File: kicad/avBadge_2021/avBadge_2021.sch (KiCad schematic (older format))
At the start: 36 parts, among them J1 AVR-ISP-6, Q1 2N3904, SW1 SW_Push_Dual, SW2 SW_SPDT, U1 ATtiny84A-SSU

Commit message: arduino code updates and manufactured v01 gerbers completed.
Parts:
- Q1: footprint TO_SOT_Packages_SMD:SOT-23 -> aerospace_badge:SOT-23-NPN
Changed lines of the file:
@@
 F 0 "Q1" H 8490 5046 50  0000 L CNN
 F 1 "2N3904" H 8490 4955 50  0000 L CNN
-F 2 "TO_SOT_Packages_SMD:SOT-23" H 8500 4925 50  0001 L CIN
+F 2 "aerospace_badge:SOT-23-NPN" H 8500 4925 50  0001 L CIN
 F 3 "https://www.fairchildsemi.com/datasheets/2N/2N3904.pdf" H 8300 5000 50  0001 L CNN
 	1    8300 5000

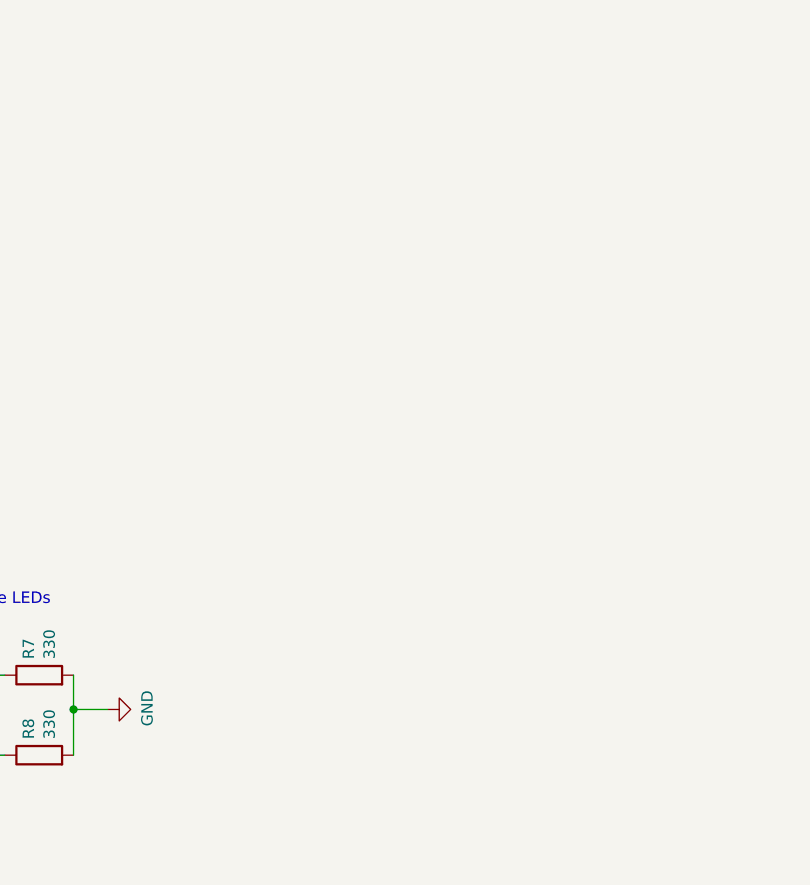
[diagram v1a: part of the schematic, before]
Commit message: arduino update to include pulsing lights as desired.
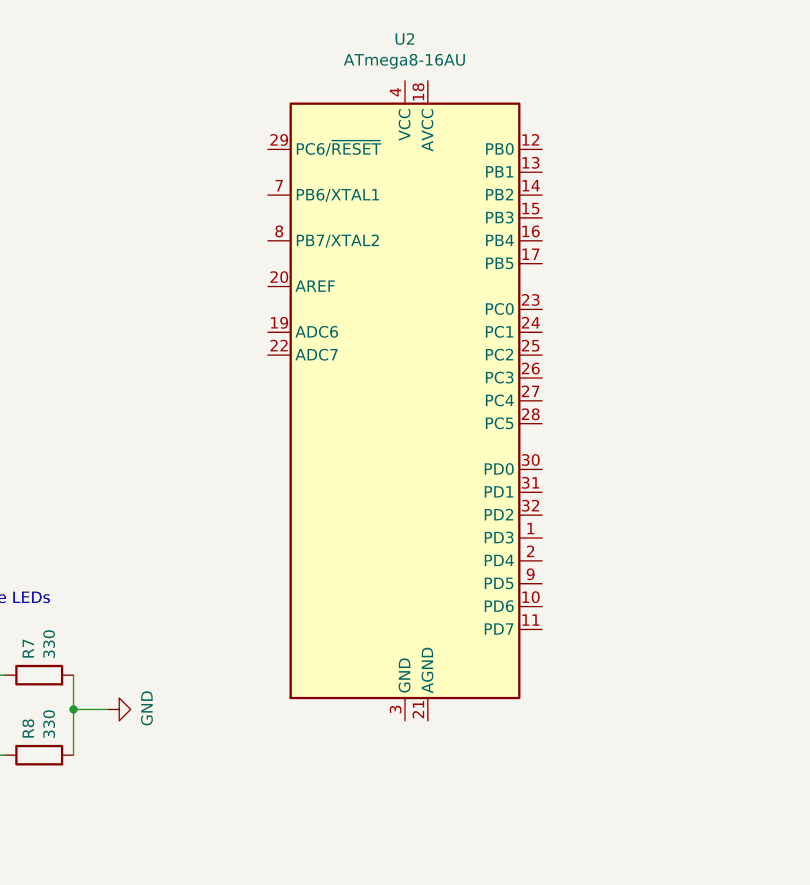
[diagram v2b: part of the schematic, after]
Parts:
- added U2: ATmega8-16AU, Package_QFP:TQFP-32_7x7mm_P0.8mm, symbol MCU_Microchip_ATmega:ATmega8-16AU
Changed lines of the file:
@@
 Wire Wire Line
 	3250 4800 3450 4800
+$Comp
+L MCU_Microchip_ATmega:ATmega8-16AU U2
+U 1 1 608E9FF1
+P 9300 2250
+F 0 "U2" H 9300 3831 50  0000 C CNN
+F 1 "ATmega8-16AU" H 9300 3740 50  0000 C CNN
+F 2 "Package_QFP:TQFP-32_7x7mm_P0.8mm" H 9300 2250 50  0001 C CIN
+F 3 "http://ww1.microchip.com/downloads/en/DeviceDoc/atmel-2486-8-bit-avr-microcontroller-atmega8_l_datasheet.pdf" H 9300 2250 50  0001 C CNN
+	1    9300 2250
+	1    0    0    -1
+$EndComp
 $EndSCHEMATC

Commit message: refactor of kicad files working through incorporation of art and new MCU design.
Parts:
- removed D1, D2: APFA3010, sunled:XZMDKCBDDG45S-9, symbol LED:APFA3010
- removed SW1: SW_Push_Dual, aerospace_badge:FSMCTTR, symbol Switch:SW_Push_Dual
- removed U1: ATtiny84A-SSU, aerospace_badge:attiny84, symbol MCU_Microchip_ATtiny:ATtiny84A-SSU
- added D1, D2: SunLED_RGB_ReverseMount, sunled:XZMDKCBDDG45S-9, symbol LED:SunLED_RGB_ReverseMount
- added D4: LED, sunled:XZDGK45WT-9, symbol Device:LED
- added P1: SerialConnector, aerospace_badge:serialConnector, symbol avBadge_symbols:SerialConnector
- added R11: 330, Resistors_SMD:R_1206_3216Metric, symbol Device:R
- added R12, R7: 10K, Resistors_SMD:R_1206_3216Metric, symbol Device:R
- added S1: OpenConnections, symbol avBadge_symbols:OpenConnections
- added VR1: TLV702, TO_SOT_Packages_SMD:SOT-23-5, symbol avBadge_symbols:TLV702
- BT1: footprint Battery:BatteryHolder_Keystone_3034_1x20mm -> aerospace_badge:BHX2-2032
- D10: renamed from D9; footprint aerospace_badge:led_in-s124ar -> sunled:XZM2CRK45WT-9
- D11: renamed from D10; footprint aerospace_badge:led_in-s124ar -> sunled:XZM2CRK45WT-9
- D12: renamed from D11; footprint aerospace_badge:led_in-s124ar -> sunled:XZM2CRK45WT-9
- U1: renamed from U2; footprint Package_QFP:TQFP-32_7x7mm_P0.8mm -> digikey-footprints:TQFP-32_7x7mm
- renumbered D4 to D5, D5 to D6, D6 to D7, D7 to D8, D8 to D9, R2 to R1, R8 to R10, R10 to R13, R11 to R14, R12 to R15, R13 to R16, R14 to R17, R15 to R18, R16 to R19, R1 to R2, R17 to R20, R4 to R3, R3 to R4, R6 to R5, R5 to R6, R7 to R8, SW2 to SW1
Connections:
- wire segments 93 -> 125
- no-connect marks 4 -> 12
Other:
- note added: "Lost Comms Interrupt"
- note added: "PCL Interrupt"
- note added: "Runway Lighting (Red, Green, Yellow)"
- note added: "UFO"
- note added: "UFO Trigger"
- note removed: "Runway Lighting (Red, Green, White)"
- moved on the sheet: BT1, C1, C2, D10, D11, D12, D6, D7, D8, D9, J1, Q1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

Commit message: v0.2 gerber builtout and sent for fabrication.
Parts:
- D10, D11, D12: footprint sunled:XZM2CRK45WT-9 -> sunled:XZMYK45WT-9
- D6, D7: footprint sunled:XZDGK45WT-9 -> sunled:XZM2CRK45WT-9
- D8, D9: footprint sunled:XZM2CRK45WT-9 -> sunled:XZDGK45WT-9
- P1: symbol avBadge_symbols:SerialConnector -> avBadge_2021-rescue:SerialConnector-avBadge_symbols
- S1: footprint (none) -> aerospace_badge:artboard
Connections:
- net GND: now also P1.~ (GND); no longer P1.3 (GND)
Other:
- note added: "G"
- note added: "R"
- note added: "Y"
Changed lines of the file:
@@
 F 0 "D6" H 7443 5567 50  0000 C CNN
 F 1 "LED" H 7443 5476 50  0000 C CNN
-F 2 "sunled:XZDGK45WT-9" H 7450 5350 50  0001 C CNN
+F 2 "sunled:XZM2CRK45WT-9" H 7450 5350 50  0001 C CNN
 F 3 "~" H 7450 5350 50  0001 C CNN
 	1    7450 5350
@@
 F 0 "D7" H 7843 5567 50  0000 C CNN
 F 1 "LED" H 7843 5476 50  0000 C CNN
-F 2 "sunled:XZDGK45WT-9" H 7850 5350 50  0001 C CNN
+F 2 "sunled:XZM2CRK45WT-9" H 7850 5350 50  0001 C CNN
 F 3 "~" H 7850 5350 50  0001 C CNN
 	1    7850 5350
@@
 F 0 "D8" H 8193 5567 50  0000 C CNN
 F 1 "LED" H 8193 5476 50  0000 C CNN
-F 2 "sunled:XZM2CRK45WT-9" H 8200 5350 50  0001 C CNN
+F 2 "sunled:XZDGK45WT-9" H 8200 5350 50  0001 C CNN
 F 3 "~" H 8200 5350 50  0001 C CNN
 	1    8200 5350
@@
 F 0 "D9" H 8543 5567 50  0000 C CNN
 F 1 "LED" H 8543 5476 50  0000 C CNN
-F 2 "sunled:XZM2CRK45WT-9" H 8550 5350 50  0001 C CNN
+F 2 "sunled:XZDGK45WT-9" H 8550 5350 50  0001 C CNN
 F 3 "~" H 8550 5350 50  0001 C CNN
 	1    8550 5350
@@
 F 0 "D10" H 8893 5567 50  0000 C CNN
 F 1 "LED" H 8893 5476 50  0000 C CNN
-F 2 "sunled:XZM2CRK45WT-9" H 8900 5350 50  0001 C CNN
+F 2 "sunled:XZMYK45WT-9" H 8900 5350 50  0001 C CNN
 F 3 "~" H 8900 5350 50  0001 C CNN
 	1    8900 5350
@@
 F 0 "D11" H 9243 5567 50  0000 C CNN
 F 1 "LED" H 9243 5476 50  0000 C CNN
-F 2 "sunled:XZM2CRK45WT-9" H 9250 5350 50  0001 C CNN
+F 2 "sunled:XZMYK45WT-9" H 9250 5350 50  0001 C CNN
 F 3 "~" H 9250 5350 50  0001 C CNN
 	1    9250 5350
@@
 F 0 "D12" H 9543 5567 50  0000 C CNN
 F 1 "LED" H 9543 5476 50  0000 C CNN
-F 2 "sunled:XZM2CRK45WT-9" H 9550 5350 50  0001 C CNN
+F 2 "sunled:XZMYK45WT-9" H 9550 5350 50  0001 C CNN
 F 3 "~" H 9550 5350 50  0001 C CNN
 	1    9550 5350
@@
 	4500 1850 4750 1850
 $Comp
-L avBadge_symbols:SerialConnector P1
+L avBadge_2021-rescue:SerialConnector-avBadge_symbols P1
 U 1 1 60B5934D
 P 3700 5500
@@
 F 0 "S1" H 5625 3925 50  0000 C CNN
 F 1 "OpenConnections" H 5625 3834 50  0000 C CNN
-F 2 "" H 5550 3700 50  0001 C CNN
+F 2 "aerospace_badge:artboard" H 5550 3700 50  0001 C CNN
 F 3 "" H 5550 3700 50  0001 C CNN
 	1    5550 3700
@@
 Wire Wire Line
 	4350 4350 5250 4350
+Text Notes 7450 6200 0    50   ~ 10
+R
+Text Notes 7800 6200 0    50   ~ 10
+R
+Text Notes 8200 6400 0    50   ~ 10
+G
+Text Notes 8550 6400 0    50   ~ 10
+G
+Text Notes 8900 6400 0    50   ~ 10
+Y
+Text Notes 9250 6400 0    50   ~ 10
+Y
+Text Notes 9550 6400 0    50   ~ 10
+Y
 $EndSCHEMATC

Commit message: incremental improvements to art, edgecuts, layout
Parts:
- removed D9: LED, sunled:XZDGK45WT-9, symbol Device:LED
- removed P1: SerialConnector, aerospace_badge:serialConnector, symbol avBadge_2021-rescue:SerialConnector-avBadge_symbols
- removed R17: 330, Resistors_SMD:R_1206_3216Metric, symbol Device:R
- removed VR1: TLV702, TO_SOT_Packages_SMD:SOT-23-5, symbol avBadge_symbols:TLV702
- added P1: SerialConnector, aerospace_badge:serialConnector, symbol avBadge_symbols:SerialConnector
- BT1: footprint aerospace_badge:BHX2-2032 -> 2479_battery_holder:2479
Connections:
- net GND: now also P1.3 (GND)
- net VCC: now also SW1.1 (A)
- net at U1.30 (PD0): now also P1.2 (RX)
- net at U1.31 (PD1): now also P1.1 (TX)
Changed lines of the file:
@@
 F 0 "BT1" H 1418 7196 50  0000 L CNN
 F 1 "Battery_Cell" H 1418 7105 50  0000 L CNN
-F 2 "aerospace_badge:BHX2-2032" V 1300 7160 50  0001 C CNN
+F 2 "2479_battery_holder:2479" V 1300 7160 50  0001 C CNN
 F 3 "~" V 1300 7160 50  0001 C CNN
 	1    1300 7100
@@
 $EndComp
 $Comp
-L Device:LED D9
-U 1 1 6083040A
-P 8550 5350
-F 0 "D9" H 8543 5567 50  0000 C CNN
-F 1 "LED" H 8543 5476 50  0000 C CNN
-F 2 "sunled:XZDGK45WT-9" H 8550 5350 50  0001 C CNN
-F 3 "~" H 8550 5350 50  0001 C CNN
-	1    8550 5350
-	0    -1   -1   0
-$EndComp
-$Comp
 L Device:LED D10
 U 1 1 60830675
@@
 $EndComp
 $Comp
-L Device:R R17
-U 1 1 60830B93
-P 8550 5800
-F 0 "R17" H 8620 5846 50  0000 L CNN
-F 1 "330" H 8620 5755 50  0000 L CNN
-F 2 "Resistors_SMD:R_1206_3216Metric" V 8480 5800 50  0001 C CNN
-F 3 "~" H 8550 5800 50  0001 C CNN
-	1    8550 5800
-	1    0    0    -1
-$EndComp
-$Comp
 L Device:R R18
 U 1 1 60830D91
@@
 	7850 5200 8200 5200
 Connection ~ 7850 5200
-Wire Wire Line
-	8200 5200 8550 5200
 Connection ~ 8200 5200
 Wire Wire Line
-	8550 5200 8900 5200
-Connection ~ 8550 5200
-Wire Wire Line
 	7450 5500 7450 5650
 Wire Wire Line
@@
 Wire Wire Line
 	8200 5500 8200 5650
-Wire Wire Line
-	8550 5500 8550 5650
 Wire Wire Line
 	8900 5500 8900 5650
@@
 	7850 5950 8200 5950
 Connection ~ 7850 5950
-Wire Wire Line
-	8200 5950 8550 5950
 Connection ~ 8200 5950
-Wire Wire Line
-	8550 5950 8900 5950
-Connection ~ 8550 5950
 Wire Wire Line
 	8200 6050 8200 5950
@@
 L power:VCC #PWR018
 U 1 1 6085AA8F
-P 2250 5700
-F 0 "#PWR018" H 2250 5550 50  0001 C CNN
-F 1 "VCC" H 2265 5873 50  0000 C CNN
-F 2 "" H 2250 5700 50  0001 C CNN
-F 3 "" H 2250 5700 50  0001 C CNN
-	1    2250 5700
-	0    1    1    0
+P 1200 6300
+F 0 "#PWR018" H 1200 6150 50  0001 C CNN
+F 1 "VCC" H 1215 6473 50  0000 C CNN
+F 2 "" H 1200 6300 50  0001 C CNN
+F 3 "" H 1200 6300 50  0001 C CNN
+	1    1200 6300
+	1    0    0    -1
 $EndComp
 $Comp
@@
 $EndComp
 $Comp
-L avBadge_symbols:TLV702 VR1
-U 1 1 609C2737
-P 1700 5800
-F 0 "VR1" H 1700 6125 50  0000 C CNN
-F 1 "TLV702" H 1700 6034 50  0000 C CNN
-F 2 "TO_SOT_Packages_SMD:SOT-23-5" H 1650 5800 50  0001 C CNN
-F 3 "" H 1650 5800 50  0001 C CNN
-	1    1700 5800
-	1    0    0    -1
-$EndComp
-Wire Wire Line
-	1200 6000 1400 6000
-Wire Wire Line
-	1200 6000 1200 6300
-Wire Wire Line
-	1200 6000 1200 5700
-Wire Wire Line
-	1200 5700 1400 5700
-Connection ~ 1200 6000
-$Comp
-L power:GND #PWR019
-U 1 1 609E0188
-P 1050 5850
-F 0 "#PWR019" H 1050 5600 50  0001 C CNN
-F 1 "GND" H 1050 5650 50  0000 C CNN
-F 2 "" H 1050 5850 50  0001 C CNN
-F 3 "" H 1050 5850 50  0001 C CNN
-	1    1050 5850
-	0    1    1    0
-$EndComp
-Wire Wire Line
-	1050 5850 1400 5850
-$Comp
-L power:GND #PWR020
-U 1 1 609E3123
-P 2200 6000
-F 0 "#PWR020" H 2200 5750 50  0001 C CNN
-F 1 "GND" H 2200 5800 50  0000 C CNN
-F 2 "" H 2200 6000 50  0001 C CNN
-F 3 "" H 2200 6000 50  0001 C CNN
-	1    2200 6000
-	0    -1   -1   0
-$EndComp
-Wire Wire Line
-	2000 6000 2200 6000
-$Comp
 L Device:R R12
 U 1 1 60A3BFDC
@@
 Wire Wire Line
 	4500 1850 4750 1850
-$Comp
-L avBadge_2021-rescue:SerialConnector-avBadge_symbols P1
-U 1 1 60B5934D
-P 3700 5500
-F 0 "P1" H 3928 5551 50  0000 L CNN
-F 1 "SerialConnector" H 3928 5460 50  0000 L CNN
-F 2 "aerospace_badge:serialConnector" H 3700 5500 50  0001 C CNN
-F 3 "" H 3700 5500 50  0001 C CNN
-	1    3700 5500
-	1    0    0    -1
-$EndComp
 $Comp
 L power:GND #PWR017
@@
 	1300 6800 1300 6700
 Wire Wire Line
-	2000 5700 2250 5700
-Wire Wire Line
 	6350 2450 6350 5000
 $Comp
@@
 Wire Wire Line
 	4350 4350 5250 4350
-Text Notes 7450 6200 0    50   ~ 10
+Text Notes 8200 6400 0    50   ~ 10
 R
-Text Notes 7800 6200 0    50   ~ 10
-R
-Text Notes 8200 6400 0    50   ~ 10
+Text Notes 7450 6400 0    50   ~ 10
 G
-Text Notes 8550 6400 0    50   ~ 10
+Text Notes 7800 6400 0    50   ~ 10
 G
 Text Notes 8900 6400 0    50   ~ 10
@@
 Text Notes 9550 6400 0    50   ~ 10
 Y
+Wire Wire Line
+	8200 5200 8900 5200
+Wire Wire Line
+	8200 5950 8900 5950
+$Comp
+L avBadge_symbols:SerialConnector P1
+U 1 1 60ADF153
+P 3700 5500
+F 0 "P1" H 3928 5551 50  0000 L CNN
+F 1 "SerialConnector" H 3928 5460 50  0000 L CNN
+F 2 "aerospace_badge:serialConnector" H 3700 5500 50  0001 C CNN
+F 3 "" H 3700 5500 50  0001 C CNN
+	1    3700 5500
+	1    0    0    -1
+$EndComp
 $EndSCHEMATC

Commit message: artwork cleanup and general tweaks. Incremental save.
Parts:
- D4: footprint sunled:XZDGK45WT-9 -> sunled:XZFBB45S-9
- S1: footprint aerospace_badge:artboard -> aerospace_badge:artboard2
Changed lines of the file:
@@
 $EndComp
-Wire Wire Line
-	7100 4650 7100 4750
 Wire Wire Line
 	6850 5950 7450 5950
@@
 Wire Wire Line
 	6850 4750 7100 4750
-Connection ~ 7100 4750
 Wire Wire Line
 	7100 4750 7100 4800
@@
 F 0 "D4" H 10143 3717 50  0000 C CNN
 F 1 "LED" H 10143 3626 50  0000 C CNN
-F 2 "sunled:XZDGK45WT-9" H 10150 3500 50  0001 C CNN
+F 2 "sunled:XZFBB45S-9" H 10150 3500 50  0001 C CNN
 F 3 "~" H 10150 3500 50  0001 C CNN
 	1    10150 3500
@@
 F 0 "S1" H 5625 3925 50  0000 C CNN
 F 1 "OpenConnections" H 5625 3834 50  0000 C CNN
-F 2 "aerospace_badge:artboard" H 5550 3700 50  0001 C CNN
+F 2 "aerospace_badge:artboard2" H 5550 3700 50  0001 C CNN
 F 3 "" H 5550 3700 50  0001 C CNN
 	1    5550 3700
@@
 	1    0    0    -1
 $EndComp
+Wire Wire Line
+	7100 4750 7100 4650
+Connection ~ 7100 4750
 $EndSCHEMATC

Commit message: v03. Updated art and everything that goes along.
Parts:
- added D9: LED, sunled:XZFBB45S-9, symbol Device:LED
- added R17: 330, Resistors_SMD:R_1206_3216Metric, symbol Device:R
- S1: footprint aerospace_badge:artboard2 -> aerospace_badge:artboard_smooth2
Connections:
- net GND: now also R17.2
- net at D4.2 (A), U1.12 (PB0): now also D9.2 (A)
- new net: D9.1 (K), R17.1
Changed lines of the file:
@@
 	1    0    0    -1
 $EndComp
-Text Notes 9800 3850 0    50   ~ 10
+Text Notes 9850 3300 0    50   ~ 10
 UFO
 Wire Wire Line
@@
 F 0 "S1" H 5625 3925 50  0000 C CNN
 F 1 "OpenConnections" H 5625 3834 50  0000 C CNN
-F 2 "aerospace_badge:artboard2" H 5550 3700 50  0001 C CNN
+F 2 "aerospace_badge:artboard_smooth2" H 5550 3700 50  0001 C CNN
 F 3 "" H 5550 3700 50  0001 C CNN
 	1    5550 3700
@@
 	7100 4750 7100 4650
 Connection ~ 7100 4750
+$Comp
+L Device:LED D9
+U 1 1 60B1DCE4
+P 9700 3500
+F 0 "D9" H 9693 3717 50  0000 C CNN
+F 1 "LED" H 9693 3626 50  0000 C CNN
+F 2 "sunled:XZFBB45S-9" H 9700 3500 50  0001 C CNN
+F 3 "~" H 9700 3500 50  0001 C CNN
+	1    9700 3500
+	0    -1   -1   0
+$EndComp
+$Comp
+L Device:R R17
+U 1 1 60B1E1BD
+P 9700 3950
+F 0 "R17" H 9770 3996 50  0000 L CNN
+F 1 "330" H 9770 3905 50  0000 L CNN
+F 2 "Resistors_SMD:R_1206_3216Metric" V 9630 3950 50  0001 C CNN
+F 3 "~" H 9700 3950 50  0001 C CNN
+	1    9700 3950
+	1    0    0    -1
+$EndComp
+$Comp
+L power:GND #PWR011
+U 1 1 60B1E737
+P 9700 4100
+F 0 "#PWR011" H 9700 3850 50  0001 C CNN
+F 1 "GND" H 9705 3927 50  0000 C CNN
+F 2 "" H 9700 4100 50  0001 C CNN
+F 3 "" H 9700 4100 50  0001 C CNN
+	1    9700 4100
+	1    0    0    -1
+$EndComp
+Wire Wire Line
+	9700 3650 9700 3800
+Wire Wire Line
+	9700 3350 10150 3350
+Connection ~ 10150 3350
 $EndSCHEMATC

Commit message: multiple changes, now on v04
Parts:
- added J2: SAO_1.69, space_shuttle_SAO:sao_1.69, symbol sao1_69:SAO_1.69
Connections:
- net GND: now also J2.2 (GND)
- net VCC: now also J2.1 (VCC)
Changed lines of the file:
@@
 	9700 3350 10150 3350
 Connection ~ 10150 3350
+$Comp
+L sao1_69:SAO_1.69 J2
+U 1 1 60C11C3B
+P 2700 5900
+F 0 "J2" H 3078 5801 50  0000 L CNN
+F 1 "SAO_1.69" H 3078 5710 50  0000 L CNN
+F 2 "space_shuttle_SAO:sao_1.69" H 2700 5900 50  0001 C CNN
+F 3 "" H 2700 5900 50  0001 C CNN
+	1    2700 5900
+	1    0    0    -1
+$EndComp
+$Comp
+L power:GND #PWR0101
+U 1 1 60C139CB
+P 2500 5900
+F 0 "#PWR0101" H 2500 5650 50  0001 C CNN
+F 1 "GND" V 2505 5772 50  0000 R CNN
+F 2 "" H 2500 5900 50  0001 C CNN
+F 3 "" H 2500 5900 50  0001 C CNN
+	1    2500 5900
+	0    1    1    0
+$EndComp
+$Comp
+L power:VCC #PWR0102
+U 1 1 60C14445
+P 2500 5800
+F 0 "#PWR0102" H 2500 5650 50  0001 C CNN
+F 1 "VCC" V 2515 5927 50  0000 L CNN
+F 2 "" H 2500 5800 50  0001 C CNN
+F 3 "" H 2500 5800 50  0001 C CNN
+	1    2500 5800
+	0    -1   -1   0
+$EndComp
+Wire Wire Line
+	2500 5800 2600 5800
+Wire Wire Line
+	2500 5900 2600 5900
 $EndSCHEMATC
